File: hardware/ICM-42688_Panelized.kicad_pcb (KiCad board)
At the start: 2 copper layers, 86 x 93 mm, 433 parts, among them J1 Conn_01x09, Q1 BSS138, Q2 BSS138, Q3 BSS138, Q4 BSS138, U1 AMS1117-3.3, U2 ICM-42688-P

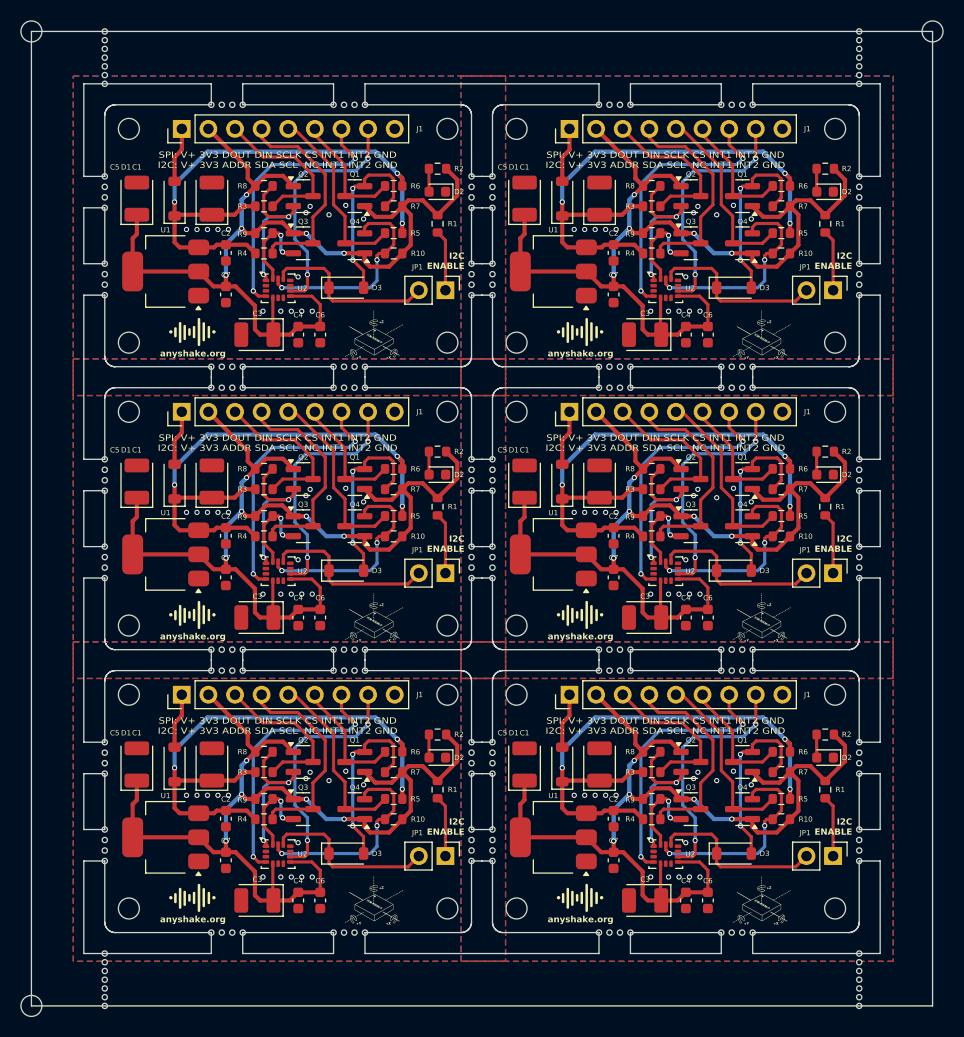
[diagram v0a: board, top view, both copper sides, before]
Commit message: fix: Fix SPI communication failure
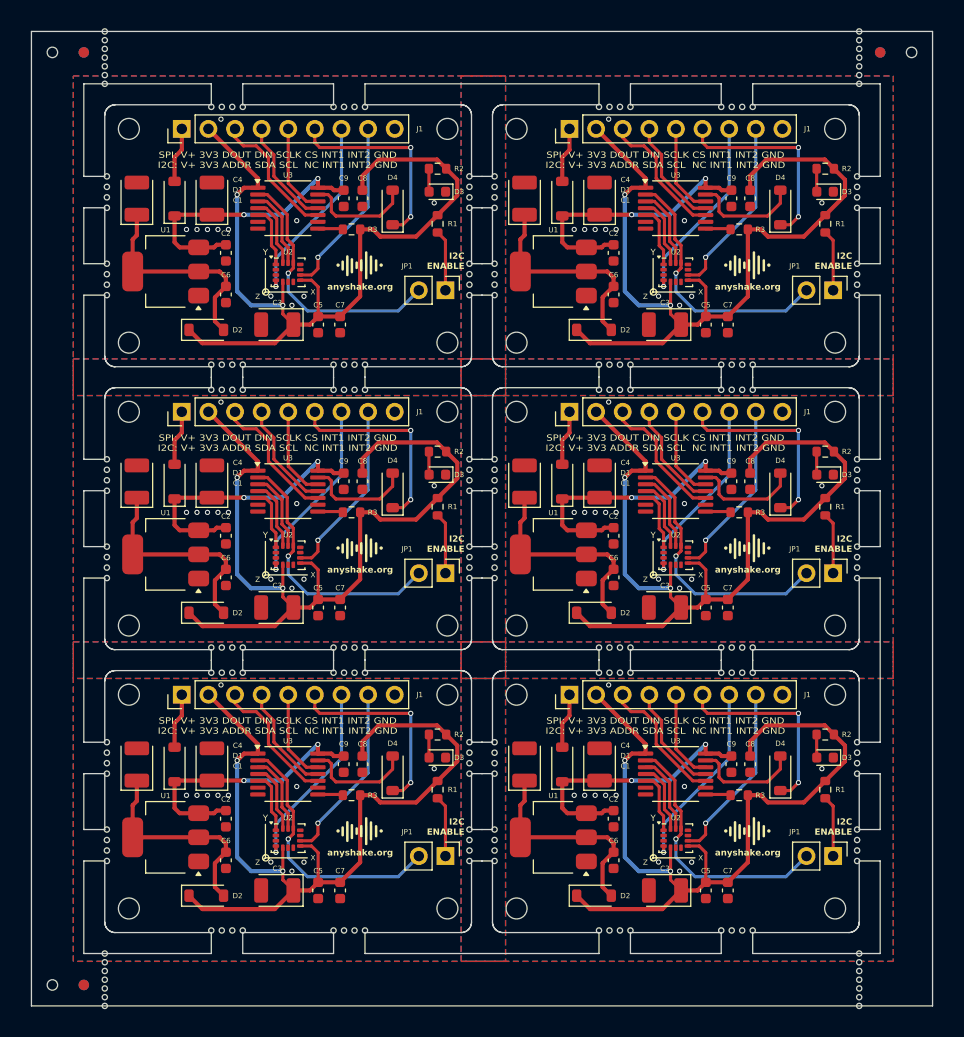
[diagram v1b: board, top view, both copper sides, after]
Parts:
- removed the C3 at (164.1, 102.9)
- removed the C3 at (127.1, 75.9)
- removed the C3 at (127.1, 102.9)
- removed the C3 at (164.1, 48.9)
- removed the C3 at (127.1, 48.9)
- removed the C3 at (164.1, 75.9)
- removed the C4 at (168.0, 75.9)
- removed the C4 at (168.0, 48.9)
- removed the C4 at (131.0, 102.9)
- removed the C4 at (131.0, 48.9)
- removed the C4 at (168.0, 102.9)
- removed the C4 at (131.0, 75.9)
- removed the C5 at (152.6, 90.0)
- removed the C5 at (115.6, 90.0)
- removed the C5 at (115.6, 63.0)
- removed the C5 at (152.6, 63.0)
- removed the C5 at (115.6, 36.0)
- removed the C5 at (152.6, 36.0)
- removed the C6 at (170.1, 75.9)
- removed the C6 at (170.1, 102.9)
- removed the C6 at (133.1, 48.9)
- removed the C6 at (170.1, 48.9)
- removed the C6 at (133.1, 102.9)
- removed the C6 at (133.1, 75.9)
- removed the C7 at (161.1, 72.1)
- removed the C7 at (124.1, 45.1)
- removed the C7 at (161.1, 99.1)
- removed the C7 at (161.1, 45.1)
- removed the C7 at (124.1, 72.1)
- removed the C7 at (124.1, 99.1)
- removed the D2 at (181.2, 62.3)
- removed the D2 at (144.2, 62.3)
- removed the D2 at (181.2, 89.3)
- removed the D2 at (144.2, 89.3)
- removed the D2 at (144.2, 35.3)
- removed the D2 at (181.2, 35.3)
- removed the D3 at (172.6, 44.5)
- removed the D3 at (135.6, 71.5)
- removed the D3 at (172.6, 71.5)
- removed the D3 at (135.6, 44.5)
- removed the D3 at (172.6, 98.5)
- removed the D3 at (135.6, 98.5)
- removed the G*** at (138.3, 49.0)
- removed the G*** at (157.9, 48.7)
- removed the G*** at (175.3, 76.0)
- removed the G*** at (157.9, 75.7)
- removed the G*** at (157.9, 102.7)
- removed the G*** at (120.9, 102.7)
- removed the G*** at (120.9, 48.7)
- removed the G*** at (120.9, 75.7)
- removed the G*** at (138.3, 76.0)
- removed the G*** at (138.3, 103.0)
- removed the G*** at (175.3, 49.0)
- removed the G*** at (175.3, 103.0)
- removed Q1 (x6), Q2 (x6), Q3 (x6), Q4 (x6): BSS138, Package_TO_SOT_SMD:SOT-23
- removed R10 (x6), R4 (x6), R5 (x6), R6 (x6), R7 (x6), R8 (x6), R9 (x6): 10k, Resistor_SMD:R_0603_1608Metric
- removed the R3 at (127.7, 90.7)
- removed the R3 at (127.7, 63.7)
- removed the R3 at (164.7, 63.7)
- removed the R3 at (127.7, 36.7)
- removed the R3 at (164.7, 36.7)
- removed the R3 at (164.7, 90.7)
- removed the U2 at (129.0, 71.5)
- removed the U2 at (166.0, 44.5)
- removed the U2 at (166.0, 98.5)
- removed the U2 at (129.0, 98.5)
- removed the U2 at (166.0, 71.5)
- removed the U2 at (129.0, 44.5)
- added C3: 2.2uF, Capacitor_Tantalum_SMD:CP_EIA-3528-12_Kemet-T, F.Cu at (166.0, 48.0)
- added C3: 2.2uF, Capacitor_Tantalum_SMD:CP_EIA-3528-12_Kemet-T, F.Cu at (129.0, 48.0)
- added C3: 2.2uF, Capacitor_Tantalum_SMD:CP_EIA-3528-12_Kemet-T, F.Cu at (129.0, 102.0)
- added C3: 2.2uF, Capacitor_Tantalum_SMD:CP_EIA-3528-12_Kemet-T, F.Cu at (129.0, 75.0)
- added C3: 2.2uF, Capacitor_Tantalum_SMD:CP_EIA-3528-12_Kemet-T, F.Cu at (166.0, 75.0)
- added C3: 2.2uF, Capacitor_Tantalum_SMD:CP_EIA-3528-12_Kemet-T, F.Cu at (166.0, 102.0)
- added C4: 22uF, Capacitor_Tantalum_SMD:CP_EIA-3528-12_Kemet-T, F.Cu at (152.6, 63.0)
- added C4: 22uF, Capacitor_Tantalum_SMD:CP_EIA-3528-12_Kemet-T, F.Cu at (115.6, 63.0)
- added C4: 22uF, Capacitor_Tantalum_SMD:CP_EIA-3528-12_Kemet-T, F.Cu at (152.6, 90.0)
- added C4: 22uF, Capacitor_Tantalum_SMD:CP_EIA-3528-12_Kemet-T, F.Cu at (115.6, 36.0)
- added C4: 22uF, Capacitor_Tantalum_SMD:CP_EIA-3528-12_Kemet-T, F.Cu at (152.6, 36.0)
- added C4: 22uF, Capacitor_Tantalum_SMD:CP_EIA-3528-12_Kemet-T, F.Cu at (115.6, 90.0)
- added C5: 0.1uF, Capacitor_SMD:C_0603_1608Metric, F.Cu at (132.9, 48.0)
- added C5: 0.1uF, Capacitor_SMD:C_0603_1608Metric, F.Cu at (169.9, 48.0)
- added C5: 0.1uF, Capacitor_SMD:C_0603_1608Metric, F.Cu at (169.9, 102.0)
- added C5: 0.1uF, Capacitor_SMD:C_0603_1608Metric, F.Cu at (132.9, 102.0)
- added C5: 0.1uF, Capacitor_SMD:C_0603_1608Metric, F.Cu at (132.9, 75.0)
- added C5: 0.1uF, Capacitor_SMD:C_0603_1608Metric, F.Cu at (169.9, 75.0)
- added C6: 0.1uF, Capacitor_SMD:C_0603_1608Metric, F.Cu at (124.1, 99.1)
- added C6: 0.1uF, Capacitor_SMD:C_0603_1608Metric, F.Cu at (124.1, 72.1)
- added C6: 0.1uF, Capacitor_SMD:C_0603_1608Metric, F.Cu at (161.1, 72.1)
- added C6: 0.1uF, Capacitor_SMD:C_0603_1608Metric, F.Cu at (161.1, 99.1)
- added C6: 0.1uF, Capacitor_SMD:C_0603_1608Metric, F.Cu at (124.1, 45.1)
- added C6: 0.1uF, Capacitor_SMD:C_0603_1608Metric, F.Cu at (161.1, 45.1)
- added C7: 0.01uF, Capacitor_SMD:C_0603_1608Metric, F.Cu at (172.0, 48.0)
- added C7: 0.01uF, Capacitor_SMD:C_0603_1608Metric, F.Cu at (135.0, 48.0)
- added C7: 0.01uF, Capacitor_SMD:C_0603_1608Metric, F.Cu at (172.0, 102.0)
- added C7: 0.01uF, Capacitor_SMD:C_0603_1608Metric, F.Cu at (135.0, 102.0)
- added C7: 0.01uF, Capacitor_SMD:C_0603_1608Metric, F.Cu at (135.0, 75.0)
- added C7: 0.01uF, Capacitor_SMD:C_0603_1608Metric, F.Cu at (172.0, 75.0)
- added C8: 0.1uF, Capacitor_SMD:C_0603_1608Metric, F.Cu at (137.1, 89.9)
- added C8: 0.1uF, Capacitor_SMD:C_0603_1608Metric, F.Cu at (174.1, 62.9)
- added C8: 0.1uF, Capacitor_SMD:C_0603_1608Metric, F.Cu at (174.1, 35.9)
- added C8: 0.1uF, Capacitor_SMD:C_0603_1608Metric, F.Cu at (137.1, 62.9)
- added C8: 0.1uF, Capacitor_SMD:C_0603_1608Metric, F.Cu at (137.1, 35.9)
- added C8: 0.1uF, Capacitor_SMD:C_0603_1608Metric, F.Cu at (174.1, 89.9)
- added C9: 0.1uF, Capacitor_SMD:C_0603_1608Metric, F.Cu at (172.3, 62.9)
- added C9: 0.1uF, Capacitor_SMD:C_0603_1608Metric, F.Cu at (135.3, 35.9)
- added C9: 0.1uF, Capacitor_SMD:C_0603_1608Metric, F.Cu at (135.3, 89.9)
- added C9: 0.1uF, Capacitor_SMD:C_0603_1608Metric, F.Cu at (172.3, 89.9)
- added C9: 0.1uF, Capacitor_SMD:C_0603_1608Metric, F.Cu at (172.3, 35.9)
- added C9: 0.1uF, Capacitor_SMD:C_0603_1608Metric, F.Cu at (135.3, 62.9)
- added D2: 1N4148, Diode_SMD:D_SOD-123, F.Cu at (122.2, 102.5)
- added D2: 1N4148, Diode_SMD:D_SOD-123, F.Cu at (159.2, 102.5)
- added D2: 1N4148, Diode_SMD:D_SOD-123, F.Cu at (122.2, 48.5)
- added D2: 1N4148, Diode_SMD:D_SOD-123, F.Cu at (122.2, 75.5)
- added D2: 1N4148, Diode_SMD:D_SOD-123, F.Cu at (159.2, 75.5)
- added D2: 1N4148, Diode_SMD:D_SOD-123, F.Cu at (159.2, 48.5)
- added D3: RED, LED_SMD:LED_0603_1608Metric, F.Cu at (144.2, 35.3)
- added D3: RED, LED_SMD:LED_0603_1608Metric, F.Cu at (181.2, 89.3)
- added D3: RED, LED_SMD:LED_0603_1608Metric, F.Cu at (144.2, 89.3)
- added D3: RED, LED_SMD:LED_0603_1608Metric, F.Cu at (181.2, 35.3)
- added D3: RED, LED_SMD:LED_0603_1608Metric, F.Cu at (181.2, 62.3)
- added D3: RED, LED_SMD:LED_0603_1608Metric, F.Cu at (144.2, 62.3)
- added D4: 1N4148, Diode_SMD:D_SOD-123, F.Cu at (140.0, 63.8)
- added D4: 1N4148, Diode_SMD:D_SOD-123, F.Cu at (177.0, 90.8)
- added D4: 1N4148, Diode_SMD:D_SOD-123, F.Cu at (140.0, 90.8)
- added D4: 1N4148, Diode_SMD:D_SOD-123, F.Cu at (177.0, 63.8)
- added D4: 1N4148, Diode_SMD:D_SOD-123, F.Cu at (177.0, 36.8)
- added D4: 1N4148, Diode_SMD:D_SOD-123, F.Cu at (140.0, 36.8)
- added G***: LOGO, AnyShake:Logo, F.Cu at (173.8, 42.3)
- added G***: LOGO, AnyShake:Logo, F.Cu at (173.8, 69.3)
- added G***: LOGO, AnyShake:Logo, F.Cu at (173.8, 96.3)
- added G***: LOGO, AnyShake:Logo, F.Cu at (136.8, 96.3)
- added G***: LOGO, AnyShake:Logo, F.Cu at (136.8, 42.3)
- added G***: LOGO, AnyShake:Logo, F.Cu at (136.8, 69.3)
- added R3: 4.7k, Resistor_SMD:R_0603_1608Metric, F.Cu at (173.1, 65.9)
- added R3: 4.7k, Resistor_SMD:R_0603_1608Metric, F.Cu at (136.1, 92.9)
- added R3: 4.7k, Resistor_SMD:R_0603_1608Metric, F.Cu at (173.1, 92.9)
- added R3: 4.7k, Resistor_SMD:R_0603_1608Metric, F.Cu at (173.1, 38.9)
- added R3: 4.7k, Resistor_SMD:R_0603_1608Metric, F.Cu at (136.1, 38.9)
- added R3: 4.7k, Resistor_SMD:R_0603_1608Metric, F.Cu at (136.1, 65.9)
- added U2: ICM-42688-P, Package_LGA:LGA-14_3x2.5mm_P0.5mm_LayoutBorder3x4y, F.Cu at (167.0, 70.0)
- added U2: ICM-42688-P, Package_LGA:LGA-14_3x2.5mm_P0.5mm_LayoutBorder3x4y, F.Cu at (130.0, 97.0)
- added U2: ICM-42688-P, Package_LGA:LGA-14_3x2.5mm_P0.5mm_LayoutBorder3x4y, F.Cu at (167.0, 43.0)
- added U2: ICM-42688-P, Package_LGA:LGA-14_3x2.5mm_P0.5mm_LayoutBorder3x4y, F.Cu at (167.0, 97.0)
- added U2: ICM-42688-P, Package_LGA:LGA-14_3x2.5mm_P0.5mm_LayoutBorder3x4y, F.Cu at (130.0, 43.0)
- added U2: ICM-42688-P, Package_LGA:LGA-14_3x2.5mm_P0.5mm_LayoutBorder3x4y, F.Cu at (130.0, 70.0)
- added U3: TXB0104PW, Package_SO:TSSOP-14_4.4x5mm_P0.65mm, F.Cu at (167.0, 90.9)
- added U3: TXB0104PW, Package_SO:TSSOP-14_4.4x5mm_P0.65mm, F.Cu at (130.0, 36.9)
- added U3: TXB0104PW, Package_SO:TSSOP-14_4.4x5mm_P0.65mm, F.Cu at (130.0, 90.9)
- added U3: TXB0104PW, Package_SO:TSSOP-14_4.4x5mm_P0.65mm, F.Cu at (130.0, 63.9)
- added U3: TXB0104PW, Package_SO:TSSOP-14_4.4x5mm_P0.65mm, F.Cu at (167.0, 36.9)
- added U3: TXB0104PW, Package_SO:TSSOP-14_4.4x5mm_P0.65mm, F.Cu at (167.0, 63.9)
- moved KiKit_FID_B_1 5.39 mm to (110.5, 22.0)
- moved KiKit_FID_B_2 5.39 mm to (186.5, 22.0)
- moved KiKit_FID_B_3 5.39 mm to (110.5, 111.0)
- moved KiKit_FID_T_1 5.39 mm to (110.5, 22.0)
- moved KiKit_FID_T_2 5.39 mm to (186.5, 22.0)
- moved KiKit_FID_T_3 5.39 mm to (110.5, 111.0)
- moved KiKit_TO_1 2.83 mm to (107.5, 22.0)
- moved KiKit_TO_2 2.83 mm to (189.5, 22.0)
- moved KiKit_TO_3 2.83 mm to (107.5, 111.0)
- moved KiKit_MB_15_1 0.20 mm to (162.7, 51.8)
- moved KiKit_MB_15_2 0.20 mm to (161.7, 51.8)
- moved KiKit_MB_15_3 0.20 mm to (160.7, 51.8)
- moved KiKit_MB_15_4 0.20 mm to (159.7, 51.8)
- moved KiKit_MB_16_1 0.20 mm to (174.3, 51.8)
- moved KiKit_MB_16_2 0.20 mm to (173.3, 51.8)
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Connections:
- net Board_0-VCC renamed Board_0-+5V
- net Board_1-VCC renamed Board_1-+5V
- net Board_2-VCC renamed Board_2-+5V
- net Board_3-VCC renamed Board_3-+5V
- net Board_4-VCC renamed Board_4-+5V
- net Board_5-VCC renamed Board_5-+5V
- R2 pad 2: Board_2-Net-(D2-A) -> Board_2-Net-(D3-A)
- R2 pad 2: Board_5-Net-(D2-A) -> Board_5-Net-(D3-A)
- R2 pad 2: Board_0-Net-(D2-A) -> Board_0-Net-(D3-A)
- R2 pad 2: Board_4-Net-(D2-A) -> Board_4-Net-(D3-A)
- R2 pad 2: Board_1-Net-(D2-A) -> Board_1-Net-(D3-A)
- R2 pad 2: Board_3-Net-(D2-A) -> Board_3-Net-(D3-A)
- U1 pad 2: Board_3-+3V3 -> Board_3-Net-(D2-A)
- U1 pad 2: Board_4-+3V3 -> Board_4-Net-(D2-A)
- U1 pad 2: Board_0-+3V3 -> Board_0-Net-(D2-A)
- U1 pad 2: Board_5-+3V3 -> Board_5-Net-(D2-A)
- U1 pad 2: Board_2-+3V3 -> Board_2-Net-(D2-A)
- U1 pad 2: Board_1-+3V3 -> Board_1-Net-(D2-A)
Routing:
- net Board_4-VDD: track 52.5 -> 26.2 mm, vias 3 -> 2
- net Board_2-VDD: track 52.5 -> 26.2 mm, vias 3 -> 2
- net Board_5-VDD: track 52.5 -> 26.2 mm, vias 3 -> 2
- net Board_0-VDD: track 52.5 -> 26.2 mm, vias 3 -> 2
- net Board_1-VDD: track 52.5 -> 26.2 mm, vias 3 -> 2
- net Board_3-VDD: track 52.5 -> 26.2 mm, vias 3 -> 2
- net Board_3-Net-(D2-A): track 2.18 -> 20.5 mm
- net Board_1-Net-(D2-A): track 2.18 -> 20.5 mm
- net Board_5-Net-(D2-A): track 2.18 -> 20.5 mm
- net Board_2-Net-(D2-A): track 2.18 -> 20.5 mm
- net Board_4-Net-(D2-A): track 2.18 -> 20.5 mm
- net Board_0-Net-(D2-A): track 2.18 -> 20.5 mm
- net Board_1-Net-(D3-A): track 17.8 -> 2.18 mm, vias 2 -> 0
- net Board_0-Net-(D3-A): track 17.8 -> 2.18 mm, vias 2 -> 0
- net Board_5-Net-(D3-A): track 17.8 -> 2.18 mm, vias 2 -> 0
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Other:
- board text added: "X"
- board text added: "Y"
- board text added: "Z"
